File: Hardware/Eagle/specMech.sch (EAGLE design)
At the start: 80 parts, among them J1 PINHD-1X8-MOLEX-SHROUD, J3 PINHD-1X8-MOLEX-SHROUD, J4 PINHD-1X8-MOLEX-SHROUD, J5 XPORT, J6 Molex 0022232081, J8 Molex 0022232081, U1 MCP23008-E/SO, U10 ADS1115, U11 MCP23008-E/SO, U12 74HC2G17TSSOP-6, U13 ISO7421DR, U14 MB85RC256, U2 MCP23008-E/SO, U3 TXB0102DCURVSSOP8, U4 MCP9808-E/MS, U5 TBD62083, U6 DS3231MZ+, U7 LTC4311ISC6TRPBF, U8 MCP23008-E/SO, U9 ADS1115

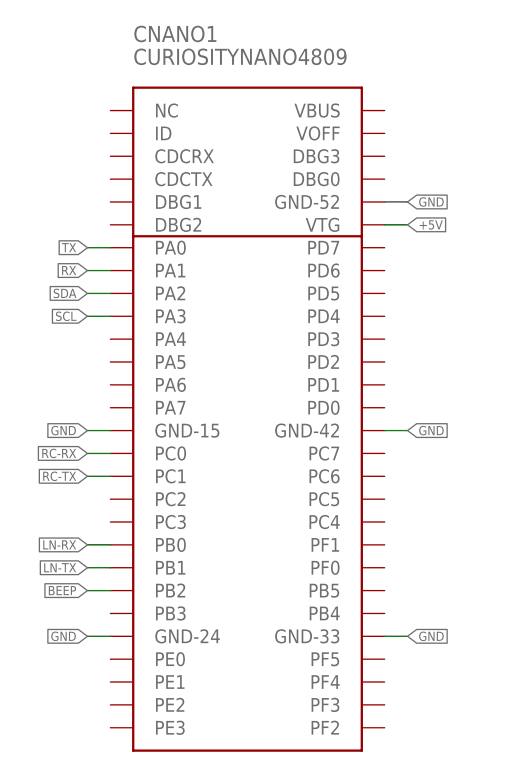
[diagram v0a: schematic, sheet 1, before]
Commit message: Connected pneumatic sensor interrupt
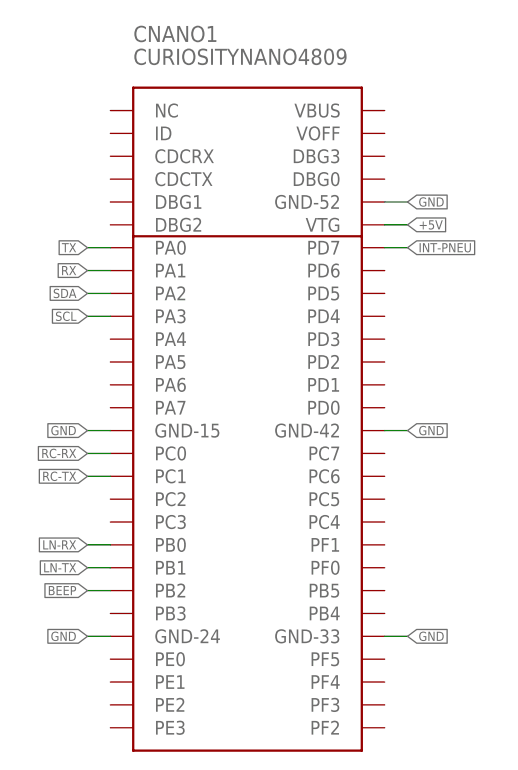
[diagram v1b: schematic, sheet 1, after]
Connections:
- net INT-PNEU: now also CNANO1.PD7
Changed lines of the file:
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@@
+</segment>
+</net>
+<net name="INT-PNEU" class="0">
+<segment>
+<pinref part="CNANO1" gate="G$1" pin="PD7"/>
+<wire x1="119.38" y1="132.08" x2="121.92" y2="132.08" width="0.1524" layer="91"/>
+<label x="121.92" y="132.08" size="1.016" layer="95" xref="yes"/>
 </segment>
 </net>

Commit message: Added Ground Overpasses
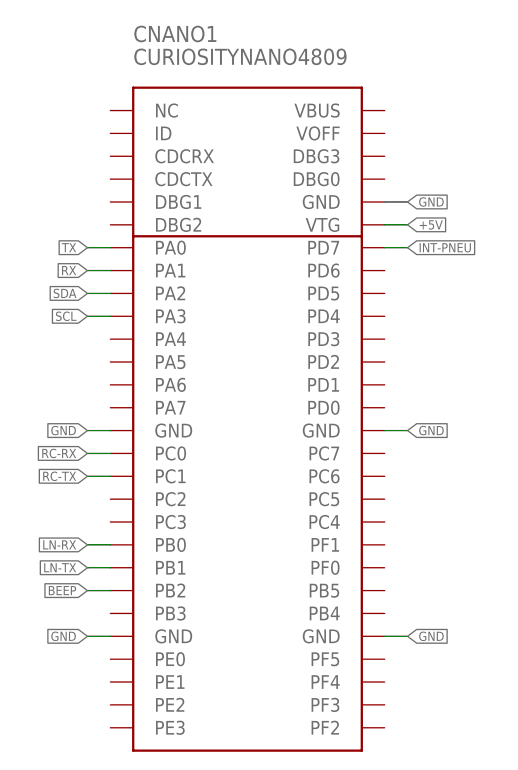
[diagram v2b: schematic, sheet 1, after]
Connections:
- net GND: now also CNANO1.GND@15, CNANO1.GND@24, CNANO1.GND@33, CNANO1.GND@42, CNANO1.GND@52; no longer CNANO1.GND-15, CNANO1.GND-24, CNANO1.GND-33, CNANO1.GND-42, CNANO1.GND-52
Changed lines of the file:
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@@
 <net name="GND" class="0">
 <segment>
-<pinref part="CNANO1" gate="G$1" pin="GND-15"/>
+<pinref part="CNANO1" gate="G$1" pin="GND@15"/>
 <wire x1="88.9" y1="111.76" x2="86.36" y2="111.76" width="0.1524" layer="91"/>
 <label x="86.36" y="111.76" size="1.016" layer="95" rot="R180" xref="yes"/>
 </segment>
 <segment>
-<pinref part="CNANO1" gate="G$1" pin="GND-42"/>
+<pinref part="CNANO1" gate="G$1" pin="GND@42"/>
 <wire x1="119.38" y1="111.76" x2="121.92" y2="111.76" width="0.1524" layer="91"/>
 <label x="121.92" y="111.76" size="1.016" layer="95" xref="yes"/>
 </segment>
 <segment>
-<pinref part="CNANO1" gate="G$1" pin="GND-24"/>
+<pinref part="CNANO1" gate="G$1" pin="GND@24"/>
 <wire x1="88.9" y1="88.9" x2="86.36" y2="88.9" width="0.1524" layer="91"/>
 <label x="86.36" y="88.9" size="1.016" layer="95" rot="R180" xref="yes"/>
 </segment>
 <segment>
-<pinref part="CNANO1" gate="G$1" pin="GND-33"/>
+<pinref part="CNANO1" gate="G$1" pin="GND@33"/>
 <wire x1="119.38" y1="88.9" x2="121.92" y2="88.9" width="0.1524" layer="91"/>
 <label x="121.92" y="88.9" size="1.016" layer="95" xref="yes"/>
 </segment>
 <segment>
-<pinref part="CNANO1" gate="G$1" pin="GND-52"/>
+<pinref part="CNANO1" gate="G$1" pin="GND@52"/>
 <wire x1="119.38" y1="137.16" x2="121.92" y2="137.16" width="0.1524" layer="91"/>
 <label x="121.92" y="137.16" size="1.016" layer="95" xref="yes"/>

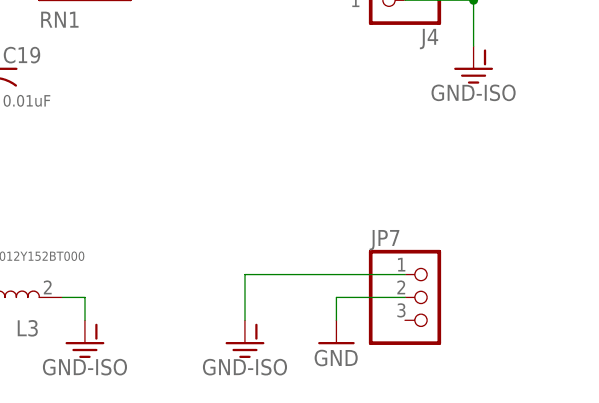
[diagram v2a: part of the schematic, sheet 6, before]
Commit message: Moved wire for USB port clearance on Nano board
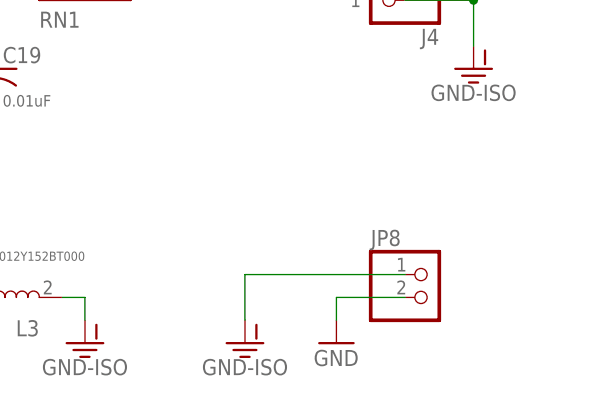
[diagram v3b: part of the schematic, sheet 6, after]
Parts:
- removed JP7: (no value), AUmlib:PINHD-1X3
- added JP8: (no value), AUmlib:PINHD-1X2
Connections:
- net GND: now also JP8.2; no longer JP7.2
- net GND-ISO: now also JP8.1; no longer JP7.1
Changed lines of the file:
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@@
 <part name="P+11" library="AUmlib" library_urn="urn:adsk.eagle:library:9166017" deviceset="+5V" device=""/>
 <part name="GND15" library="AUmlib" library_urn="urn:adsk.eagle:library:9166017" deviceset="GND" device=""/>
-<part name="JP7" library="AUmlib" library_urn="urn:adsk.eagle:library:9166017" deviceset="PINHD-1X3" device="" package3d_urn="urn:adsk.eagle:package:21589412/1"/>
 <part name="GND-ISO4" library="AUmlib" library_urn="urn:adsk.eagle:library:9166017" deviceset="GND-ISO" device=""/>
 <part name="GND43" library="AUmlib" library_urn="urn:adsk.eagle:library:9166017" deviceset="GND" device=""/>
@@
 <part name="GND-ISO9" library="AUmlib" library_urn="urn:adsk.eagle:library:9166017" deviceset="GND-ISO" device=""/>
 <part name="BO1" library="AUmlib" library_urn="urn:adsk.eagle:library:9166017" deviceset="MMA8451BREAKOUT" device="" package3d_urn="urn:adsk.eagle:package:24524265/4"/>
+<part name="JP8" library="AUmlib" library_urn="urn:adsk.eagle:library:9166017" deviceset="PINHD-1X2" device="" package3d_urn="urn:adsk.eagle:package:15461696/1"/>
 </parts>
 <sheets>
@@
 <attribute name="DRAWING_NAME" x="190.5" y="19.05" size="2.54" layer="94"/>
 </instance>
-<instance part="JP7" gate="A" x="167.64" y="60.96" smashed="yes">
-<attribute name="NAME" x="161.29" y="66.675" size="1.778" layer="95"/>
-<attribute name="VALUE" x="161.29" y="53.34" size="1.778" layer="96"/>
-</instance>
 <instance part="GND-ISO4" gate="G$1" x="147.32" y="55.88" smashed="yes">
 <attribute name="VALUE" x="147.32" y="54.102" size="1.778" layer="96" align="top-center"/>
@@
 <instance part="GND-ISO9" gate="G$1" x="48.26" y="160.02" smashed="yes">
 <attribute name="VALUE" x="48.26" y="158.242" size="1.778" layer="96" align="top-center"/>
+</instance>
+<instance part="JP8" gate="G$1" x="167.64" y="60.96" smashed="yes">
+<attribute name="NAME" x="161.29" y="66.675" size="1.778" layer="95"/>
+<attribute name="VALUE" x="161.29" y="55.88" size="1.778" layer="96"/>
 </instance>
 </instances>
@@
 </segment>
 <segment>
-<pinref part="JP7" gate="A" pin="2"/>
 <wire x1="165.1" y1="60.96" x2="157.48" y2="60.96" width="0.1524" layer="91"/>
 <wire x1="157.48" y1="60.96" x2="157.48" y2="58.42" width="0.1524" layer="91"/>
 <pinref part="GND43" gate="1" pin="GND"/>
+<pinref part="JP8" gate="G$1" pin="2"/>
 </segment>
 </net>
@@
 </segment>
 <segment>
-<pinref part="JP7" gate="A" pin="1"/>
 <wire x1="165.1" y1="63.5" x2="147.32" y2="63.5" width="0.1524" layer="91"/>
 <wire x1="147.32" y1="63.5" x2="147.32" y2="58.42" width="0.1524" layer="91"/>
 <pinref part="GND-ISO4" gate="G$1" pin="GND-ISO"/>
-</segment>
-<segment>
+<pinref part="JP8" gate="G$1" pin="1"/>
+</segment>
+<segment>

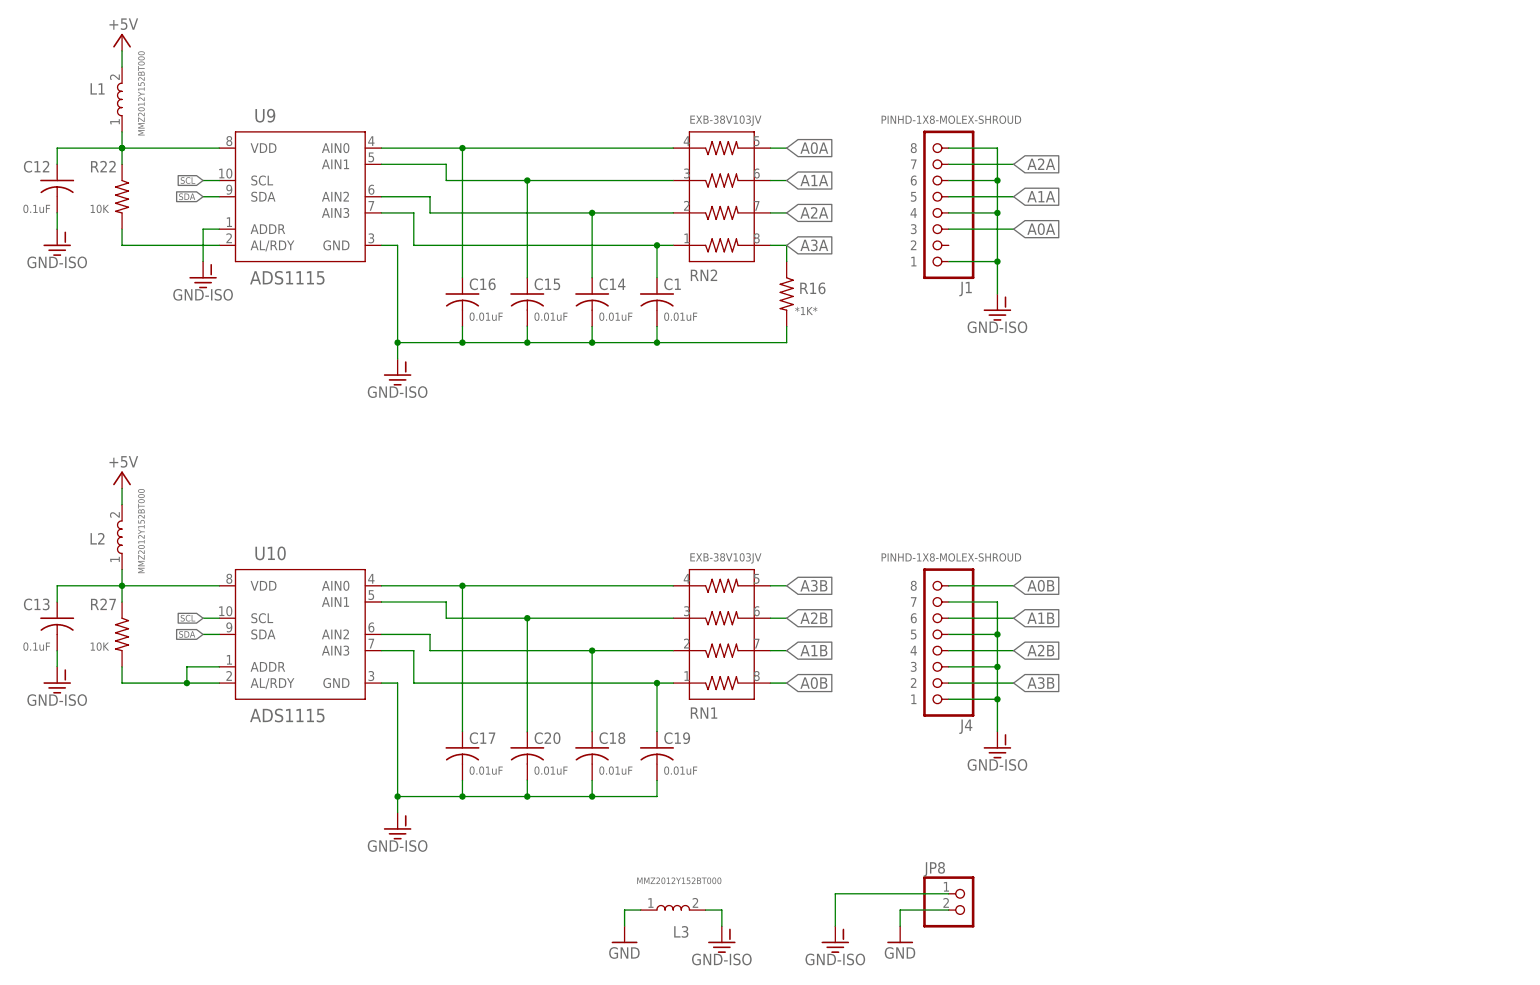
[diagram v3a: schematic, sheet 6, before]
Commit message: Partitioned grounds (removed analog ground)
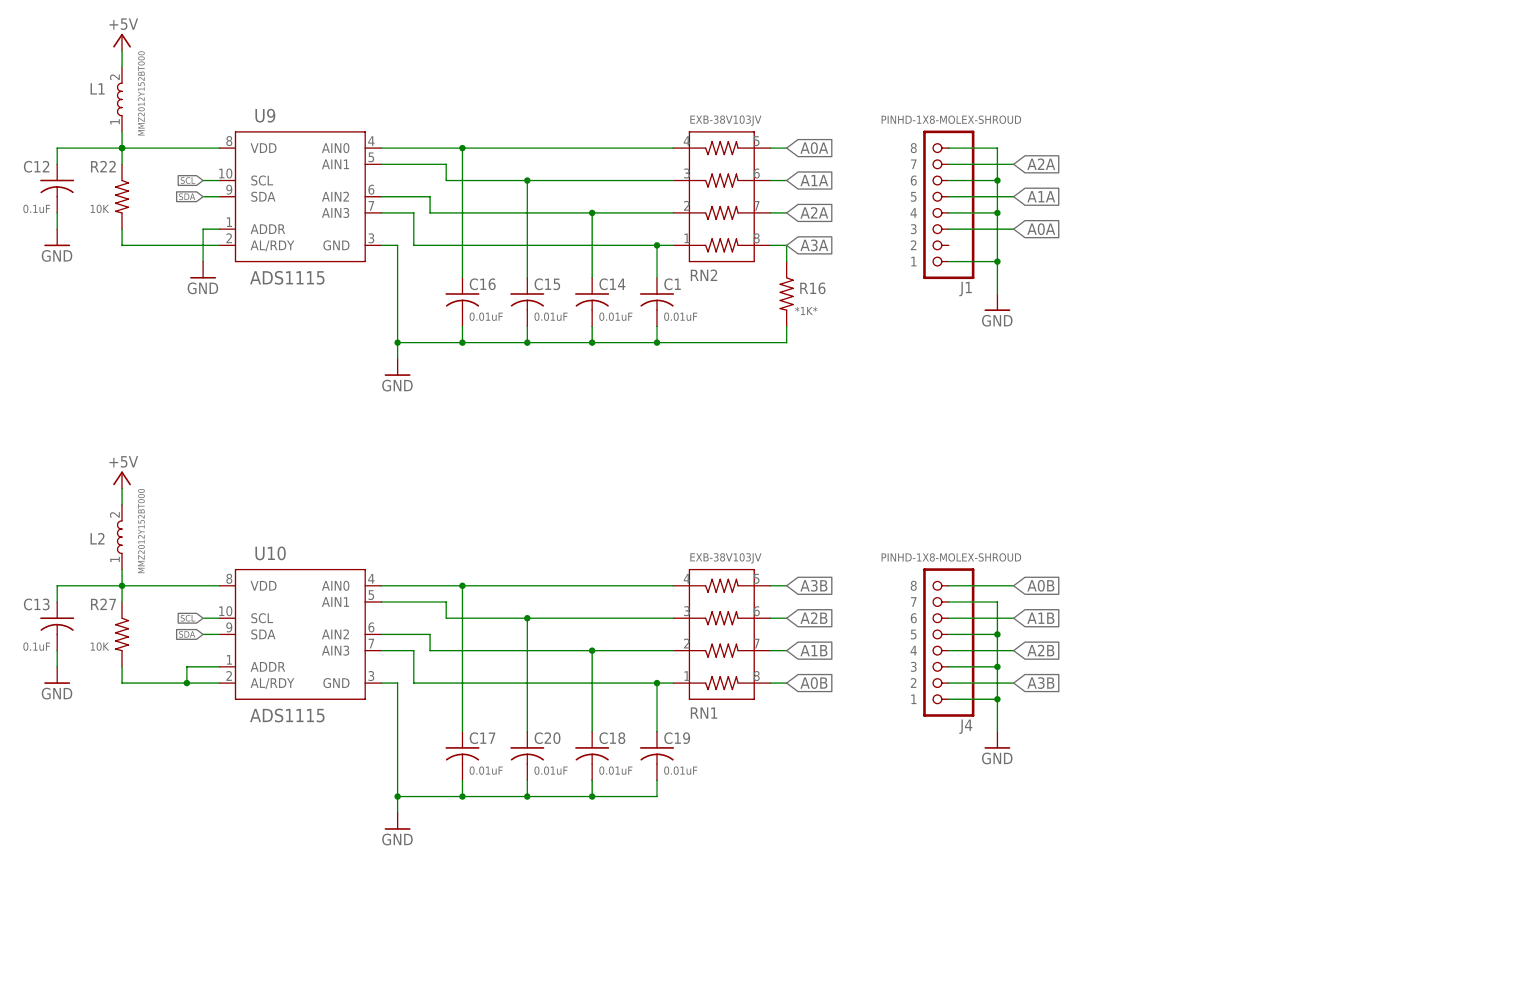
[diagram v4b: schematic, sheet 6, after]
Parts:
- removed JP8: (no value), AUmlib:PINHD-1X2
- removed L3: MMZ2012Y152BT000, AUmlib:MMZ2012Y152BT000
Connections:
- removed net GND-ISO: C1.2, C12.2, C13.2, C14.2, C15.2, C16.2, C17.2, C18.2, C19.2, C20.2, J1.1, J1.4, J1.6, J1.8, J4.1, J4.3, J4.5, J4.7, JP8.1, L3.2, R16.2, U10.GND, U9.ADDR, U9.GND
- net GND: now also C1.2, C12.2, C13.2, C14.2, C15.2, C16.2, C17.2, C18.2, C19.2, C20.2, J1.1, J1.4, J1.6, J1.8, J4.1, J4.3, J4.5, J4.7, R16.2, U10.GND, U9.ADDR, U9.GND; no longer JP8.2, L3.1

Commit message: Used later version of XPORT-2
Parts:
- removed L2: MMZ2012Y152BT000, AUmlib:MMZ2012Y152BT000
- J7: value XPORT -> (none)
- renumbered J5 to J7
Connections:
- removed net N$6: C13.1, L2.1, R27.1, U10.VDD
- removed net N$7: C12.1, L1.1, R22.1, U9.VDD
- new net FILT5V: C12.1, C13.1, C21.1, L1.1, R22.1, R27.1, U10.VDD, U11.VDD, U9.VDD
- net +5V: no longer C21.1, L2.2, U11.VDD
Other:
- moved on the sheet: C1, C12, C13, C14, C15, C16, C17, C18, C19, C20, J1, J4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

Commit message: Finish for the day
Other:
- note added: "0.01 uF filter caps. 200 V, low ESR, from chassis ground to signal ground and from chassis ground to +3.3 V. Spikes from chassis ground are shared to maintain 3.3 V signaling."
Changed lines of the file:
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@@
 <setting verticaltext="up"/>
 </settings>
-<grid distance="0.1" unitdist="inch" unit="inch" style="lines" multiple="1" display="yes" altdistance="0.01" altunitdist="inch" altunit="inch"/>
+<grid distance="0.1" unitdist="inch" unit="inch" style="lines" multiple="1" display="no" altdistance="0.01" altunitdist="inch" altunit="inch"/>
 <layers>
 <layer number="1" name="Top" color="4" fill="1" visible="no" active="no"/>
@@
 <text x="200.66" y="119.38" size="1.778" layer="250">A side is +3.3V
 B side is +5V</text>
+<text x="132.08" y="53.34" size="1.27" layer="250">0.01 uF filter caps. 200 V, low ESR,
+from chassis ground to signal ground
+and from chassis ground to +3.3 V.
+Spikes from chassis ground are shared
+to maintain 3.3 V signaling.</text>
 </plain>
 <instances>

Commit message: Connected VOFF to GND
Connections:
- net GND: now also CNANO1.VOFF
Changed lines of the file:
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@@
 <label x="121.92" y="137.16" size="1.016" layer="95" xref="yes"/>
+</segment>
+<segment>
+<pinref part="CNANO1" gate="G$1" pin="VOFF"/>
+<wire x1="119.38" y1="144.78" x2="121.92" y2="144.78" width="0.1524" layer="91"/>
+<label x="121.92" y="144.78" size="1.016" layer="95" xref="yes"/>
 </segment>
 </net>
